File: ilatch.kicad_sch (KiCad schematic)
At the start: 11 parts, among them Q1 PNP, U25 74HC273, U26 74HC14, U27 74HC541, U28 74HC4075

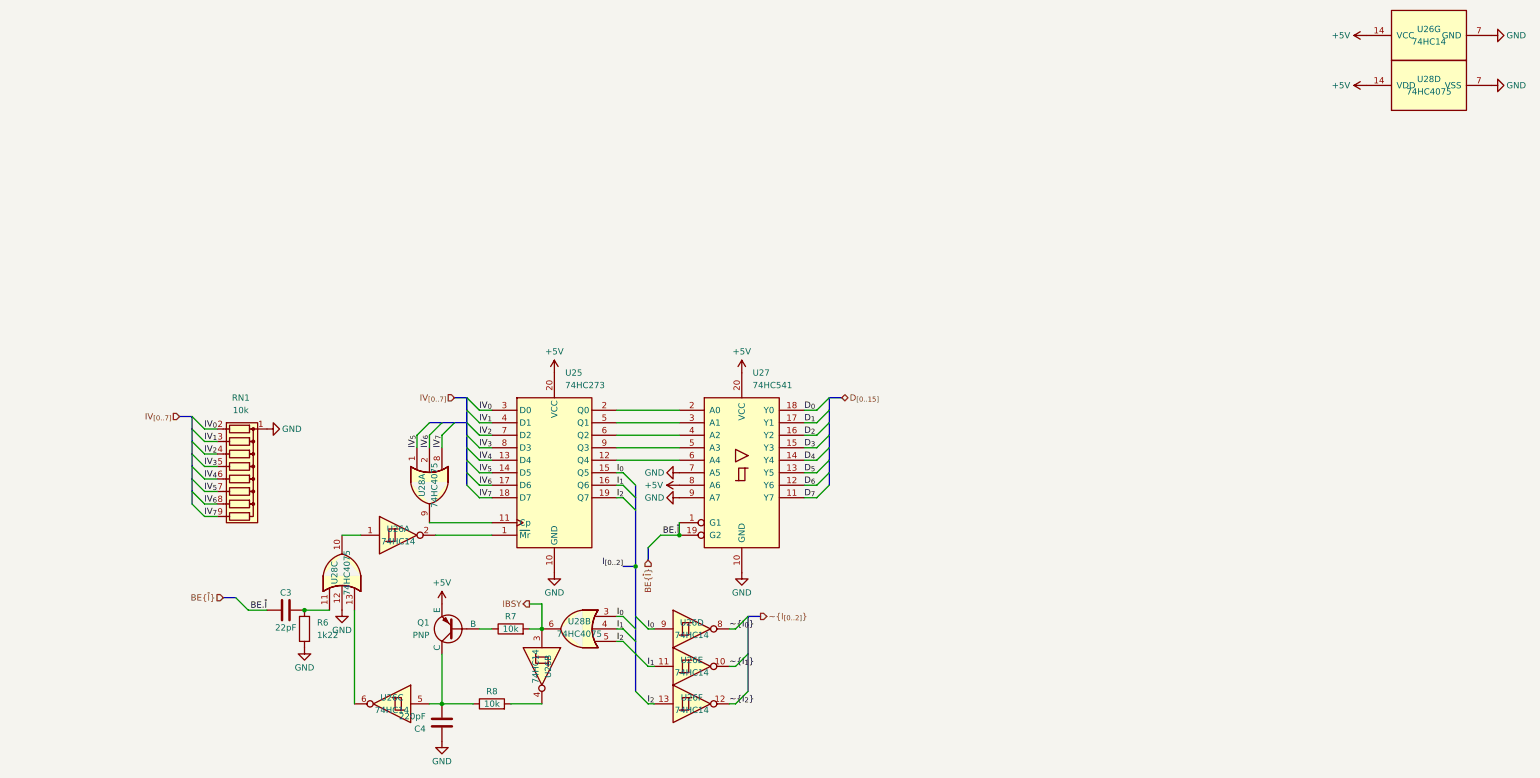
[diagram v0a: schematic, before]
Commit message: finished scheme, footprints not completely assigned yet
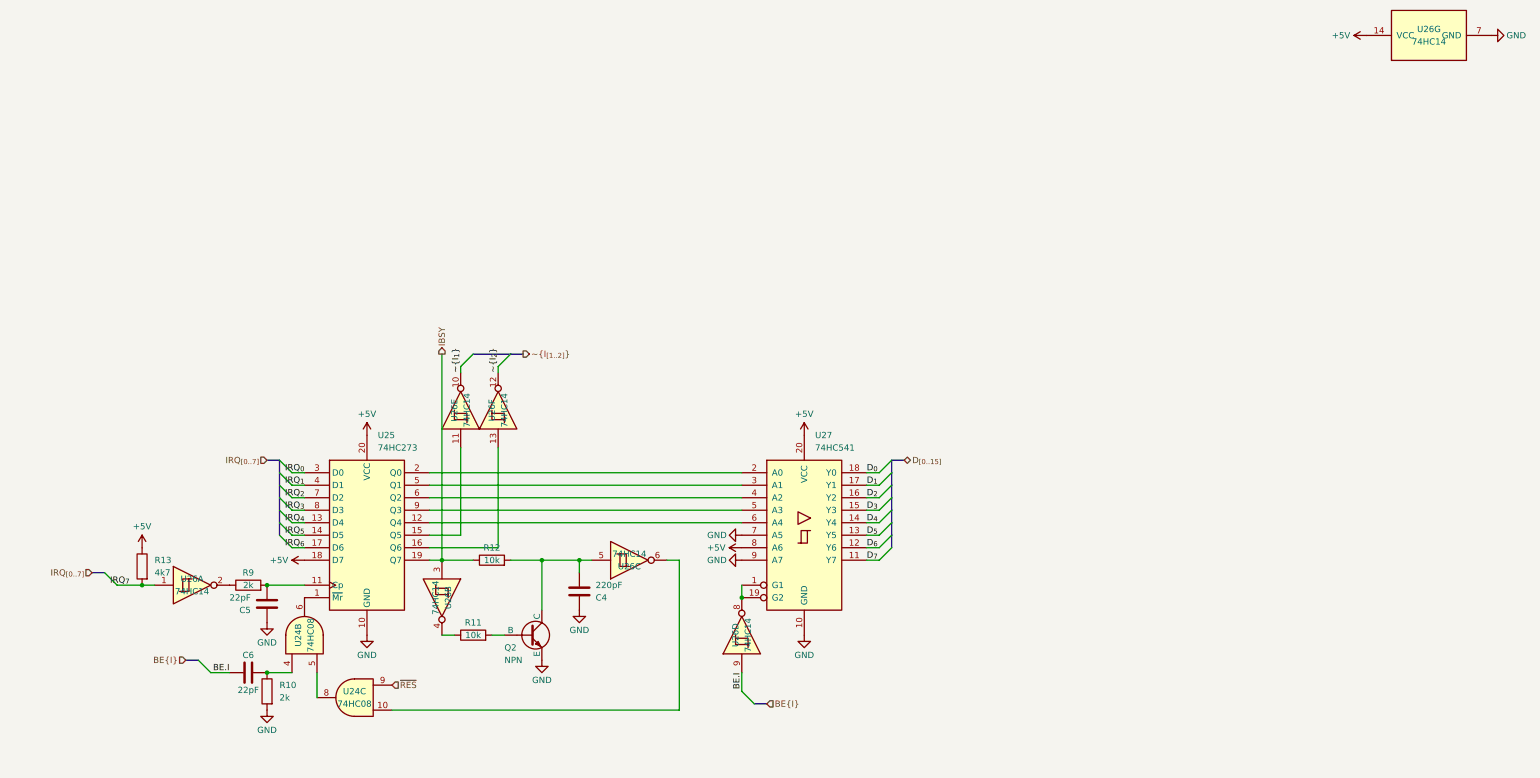
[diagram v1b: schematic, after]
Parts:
- removed C3: 22pF, Capacitor_THT:C_Disc_P2.54mm, symbol Device:C
- removed Q1: PNP, symbol Simulation_SPICE:PNP
- removed R6: 1k22, Resistor_THT:R_Axial_DIN0207_L6.3mm_D2.5mm_P2.54mm_Vertical, symbol Device:R
- removed R7, R8: 10k, Resistor_THT:R_Axial_DIN0207_L6.3mm_D2.5mm_P2.54mm_Vertical, symbol Device:R
- removed RN1: 10k, Resistor_THT:R_Array_SIP9, symbol Device:R_Network08
- removed U28: 74HC4075, Package_DIP:DIP-14_W7.62mm_Socket, symbol 4xxx:4075
- added C5, C6: 22pF, Capacitor_THT:C_Disc_P2.54mm, symbol Device:C
- added Q2: NPN, symbol Simulation_SPICE:NPN
- added R10, R9: 2k, Resistor_THT:R_Axial_DIN0207_L6.3mm_D2.5mm_P2.54mm_Vertical, symbol Device:R
- added R11, R12: 10k, Resistor_THT:R_Axial_DIN0207_L6.3mm_D2.5mm_P2.54mm_Vertical, symbol Device:R
- added R13: 4k7, Resistor_THT:R_Axial_DIN0207_L6.3mm_D2.5mm_P2.54mm_Vertical, symbol Device:R
- added U24: 74HC08, Package_DIP:DIP-14_W7.62mm_Socket, symbol 74xx:74LS08
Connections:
- net IV_{7} is gone; now on net +5V: U25.18 (D7)
- net ~{I_{0}} is gone; now on an unnamed net: U26.8
- net +5V: now also R13.1
- net GND: now also C5.1, Q2.3 (E), R10.2
- net IBSY: now also U25.19 (Q7), R12.1
- net IRQ_{7}: now reaches U26.1
- net IRQ_{7}: now also R13.2
- net at U26.2: now also R9.1; no longer U25.1 (~{Mr})
- net at U26.6: now also U24.10
- net at U26.4: now also R11.1
- net at C4.2, U26.5: now also Q2.1 (C), R12.2
- net at U25.11 (Cp): now also C5.2, R9.2
- net BE.~{I}: no longer names the net of U27.1 (G1), U27.19 (G2)
- net IV_{0} renamed IRQ_{0}
- net IV_{1} renamed IRQ_{1}
- net IV_{2} renamed IRQ_{2}
- net IV_{3} renamed IRQ_{3}
- net IV_{4} renamed IRQ_{4}
- net IV_{5} renamed IRQ_{5}
- net IV_{6} renamed IRQ_{6}
- net I_{0}: no longer names the net of U25.15 (Q5)
- net I_{0}: now also U26.11; no longer U26.9
- net I_{1}: no longer names the net of U25.16 (Q6)
- net I_{1}: now also U26.13; no longer U26.11
- removed net I_{2}: U25.19 (Q7), U26.13
- new net: C6.2, R10.1, U24.4
- new net: U24.5, U24.8
- new net: Q2.2 (B), R11.2
- new net: U24.6, U25.1 (~{Mr})
- new net BE.I: C6.1, U26.9
- new net ~{RES}: U24.9
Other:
- moved on the sheet: C4, U25, U26A, U26B, U26C, U26D, U26E, U26F, U27

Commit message: done the pcb layout + added the 1M ram bank project
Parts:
- C4, C5, C6: footprint Capacitor_THT:C_Disc_P2.54mm -> Capacitor_THT:C_Disc_D3.0mm_W1.6mm_P2.54mm
- Q2: footprint (none) -> Package_TO_SOT_THT:TO-92
- U24, U26: footprint Package_DIP:DIP-14_W7.62mm_Socket -> Package_DIP:DIP-14_W7.62mm
- U25: footprint (none) -> Package_DIP:DIP-20_W7.62mm
- U27: footprint Package_DIP:DIP-20_W7.62mm_Socket -> Package_DIP:DIP-20_W7.62mm
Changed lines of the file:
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@@
 			)
 		)
-		(property "Footprint" "Package_DIP:DIP-14_W7.62mm_Socket"
+		(property "Footprint" "Package_DIP:DIP-14_W7.62mm"
 			(at 78.74 111.76 0)
 			(effects
@@
 			)
 		)
-		(property "Footprint" "Capacitor_THT:C_Disc_P2.54mm"
+		(property "Footprint" "Capacitor_THT:C_Disc_D3.0mm_W1.6mm_P2.54mm"
 			(at 93.98 128.5748 0)
 			(effects
@@
 			)
 		)
-		(property "Footprint" "Package_DIP:DIP-14_W7.62mm_Socket"
+		(property "Footprint" "Package_DIP:DIP-14_W7.62mm"
 			(at 129.54 114.3 0)
 			(effects
@@
 			)
 		)
-		(property "Footprint" "Package_DIP:DIP-14_W7.62mm_Socket"
+		(property "Footprint" "Package_DIP:DIP-14_W7.62mm"
 			(at 111.76 134.62 0)
 			(effects
@@
 			)
 		)
-		(property "Footprint" "Package_DIP:DIP-14_W7.62mm_Socket"
+		(property "Footprint" "Package_DIP:DIP-14_W7.62mm"
 			(at 133.35 76.2 0)
 			(effects
@@
 			)
 		)
-		(property "Footprint" "Capacitor_THT:C_Disc_P2.54mm"
+		(property "Footprint" "Capacitor_THT:C_Disc_D3.0mm_W1.6mm_P2.54mm"
 			(at 156.5148 109.22 0)
 			(effects
@@
 			)
 		)
-		(property "Footprint" ""
+		(property "Footprint" "Package_TO_SOT_THT:TO-92"
 			(at 210.82 121.92 0)
 			(effects
@@
 			)
 		)
-		(property "Footprint" "Package_DIP:DIP-14_W7.62mm_Socket"
+		(property "Footprint" "Package_DIP:DIP-14_W7.62mm"
 			(at 140.97 76.2 0)
 			(effects
@@
 			)
 		)
-		(property "Footprint" "Package_DIP:DIP-20_W7.62mm_Socket"
+		(property "Footprint" "Package_DIP:DIP-20_W7.62mm"
 			(at 203.2 101.6 0)
 			(effects
@@
 			)
 		)
-		(property "Footprint" "Capacitor_THT:C_Disc_P2.54mm"
+		(property "Footprint" "Capacitor_THT:C_Disc_D3.0mm_W1.6mm_P2.54mm"
 			(at 94.9452 111.76 0)
 			(effects
@@
 			)
 		)
-		(property "Footprint" "Package_DIP:DIP-14_W7.62mm_Socket"
+		(property "Footprint" "Package_DIP:DIP-14_W7.62mm"
 			(at 190.5 121.92 0)
 			(effects
@@
 			)
 		)
-		(property "Footprint" ""
+		(property "Footprint" "Package_DIP:DIP-20_W7.62mm"
 			(at 114.3 101.6 0)
 			(effects
@@
 			)
 		)
-		(property "Footprint" "Package_DIP:DIP-14_W7.62mm_Socket"
+		(property "Footprint" "Package_DIP:DIP-14_W7.62mm"
 			(at 101.6 121.92 0)
 			(effects
@@
 			)
 		)
-		(property "Footprint" "Package_DIP:DIP-14_W7.62mm_Socket"
+		(property "Footprint" "Package_DIP:DIP-14_W7.62mm"
 			(at 167.64 106.68 0)
 			(effects
@@
 			)
 		)
-		(property "Footprint" "Package_DIP:DIP-14_W7.62mm_Socket"
+		(property "Footprint" "Package_DIP:DIP-14_W7.62mm"
 			(at 330.2 0 0)
 			(effects

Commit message: first commit: scheme ok [decoder]: 	- new spv. address space [mmu]: 	- removed pidreg 	- switched back to 8Kb mmu rams [ram/peripherals]: 	- added ground pins to connectors [misc]: 	- added DMA support 	- added clock halfer
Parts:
- added unit 3 of U31
- added unit 4 of U31
- added unit 5 of U31
- renumbered U24 to U31
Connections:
- net +5V: now also U31.10, U31.12, U31.13, U31.14 (VCC), U31.9
- net GND: now also U31.7 (GND)
- net ~{RES}: now also U31.4; no longer U31.9
- net at C6.2, R10.1: now also U31.1; no longer U31.4
- net at U26.6: now also U31.5; no longer U31.10
- net at U25.1 (~{Mr}): now also U31.3; no longer U31.6
- new net: U31.2, U31.6
- no-connect marks 0 -> 2

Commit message: applied sf68 & ps2 fixes stash from master
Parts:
- renumbered C6 to C5, R10 to R14
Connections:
- net +5V: now also R14.1
- net GND: no longer R14.2
- net at C5.2, U31.1: now also R14.2; no longer R14.1
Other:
- moved on the sheet: C5, R14
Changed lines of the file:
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@@
 	)
 	(junction
-		(at 322.58 40.64)
+		(at 129.54 106.68)
 		(diameter 0)
 		(color 0 0 0 0)
 	)
 	(junction
-		(at 93.98 129.54)
-		(diameter 0)
-		(color 0 0 0 0)
-	)
-	(junction
-		(at 129.54 106.68)
+		(at 93.98 139.7)
 		(diameter 0)
 		(color 0 0 0 0)
@@
 	)
 	(bus_entry
-		(at 80.01 127)
+		(at 80.01 137.16)
 		(size 2.54 2.54)
 		(stroke
@@
 	(wire
 		(pts
-			(xy 93.98 129.54) (xy 99.06 129.54)
+			(xy 93.98 139.7) (xy 99.06 139.7)
 		)
 		(stroke
@@
 	(wire
 		(pts
+			(xy 99.06 129.54) (xy 99.06 139.7)
+		)
+		(stroke
+			(width 0)
+			(type default)
+		)
+	)
+	(wire
+		(pts
 			(xy 127 101.6) (xy 133.35 101.6)
 		)
@@
 	(bus
 		(pts
-			(xy 77.47 127) (xy 80.01 127)
+			(xy 77.47 137.16) (xy 80.01 137.16)
 		)
 		(stroke
@@
 	(wire
 		(pts
-			(xy 82.55 129.54) (xy 86.36 129.54)
+			(xy 82.55 139.7) (xy 86.36 139.7)
 		)
 		(stroke
@@
 	)
 	(label "BE.I"
-		(at 86.36 129.54 180)
+		(at 86.36 139.7 180)
 		(effects
 			(font
@@
 	(hierarchical_label "BE{I}"
 		(shape input)
-		(at 77.47 127 180)
+		(at 77.47 137.16 180)
 		(effects
 			(font
@@
 	(symbol
 		(lib_id "Device:R")
-		(at 93.98 133.35 0)
+		(at 93.98 135.89 0)
 		(mirror y)
 		(unit 1)
@@
 		(on_board yes)
 		(dnp no)
-		(property "Reference" "R10"
-			(at 96.52 132.0799 0)
+		(property "Reference" "R14"
+			(at 96.52 134.6199 0)
 			(effects
 				(font
@@
 		)
 		(property "Value" "2k"
-			(at 96.52 134.6199 0)
+			(at 96.52 137.1599 0)
 			(effects
 				(font
@@
 		)
 		(property "Footprint" "Resistor_THT:R_Axial_DIN0207_L6.3mm_D2.5mm_P2.54mm_Vertical"
-			(at 95.758 133.35 90)
+			(at 95.758 135.89 90)
 			(effects
 				(font
@@
 			)
 		)
-		(property "Datasheet" "~"
-			(at 93.98 133.35 0)
+		(property "Datasheet" ""
+			(at 93.98 135.89 0)
 			(effects
 				(font
@@
 			)
 		)
-		(property "Description" "Resistor"
-			(at 93.98 133.35 0)
+		(property "Description" ""
+			(at 93.98 135.89 0)
 			(effects
 				(font
@@
 	)
 	(symbol
-		(lib_id "power:GND")
-		(at 93.98 137.16 0)
-		(mirror y)
-		(unit 1)
-		(exclude_from_sim no)
-		(in_bom yes)
-		(on_board yes)
-		(dnp no)
-		(property "Reference" "#PWR097"
-			(at 93.98 143.51 0)
-			(effects
-				(font
-					(size 1.27 1.27)
-				)
-				(hide yes)
-			)
-		)
-		(property "Value" "GND"
-			(at 93.98 141.224 0)
-			(effects
-				(font
-					(size 1.27 1.27)
-				)
-			)
-		)
-		(property "Footprint" ""
-			(at 93.98 137.16 0)
-			(effects
-				(font
-					(size 1.27 1.27)
-				)
-				(hide yes)
-			)
-		)
-		(property "Datasheet" ""
-			(at 93.98 137.16 0)
-			(effects
-				(font
-					(size 1.27 1.27)
-				)
-				(hide yes)
-			)
-		)
-		(property "Description" "Power symbol creates a global label with name \"GND\" , ground"
-			(at 93.98 137.16 0)
-			(effects
-				(font
-					(size 1.27 1.27)
-				)
-				(hide yes)
-			)
-		)
-		(pin "1"
-		)
-		(instances
-			(project "SCRM6816"
-				(path "/56448118-82b3-4e1c-bda3-84d63e01a14a/024e6e5e-a156-416a-80e5-bb61019b3b6b"
-					(reference "#PWR097")
-					(unit 1)
-				)
-			)
-		)
-	)
-	(symbol
 		(lib_id "power:+9V")
 		(at 101.6 106.68 90)
@@
 	(symbol
 		(lib_id "Device:C")
-		(at 90.17 129.54 90)
+		(at 90.17 139.7 90)
 		(unit 1)
 		(exclude_from_sim no)
@@
 		(on_board yes)
 		(dnp no)
-		(property "Reference" "C6"
-			(at 90.17 125.984 90)
+		(property "Reference" "C5"
+			(at 90.17 136.144 90)
 			(effects
 				(font
@@
 		)
 		(property "Value" "22pF"
-			(at 90.17 133.096 90)
+			(at 90.17 143.256 90)
 			(effects
 				(font
@@
 		)
 		(property "Footprint" "Capacitor_THT:C_Disc_D3.0mm_W1.6mm_P2.54mm"
-			(at 93.98 128.5748 0)
+			(at 93.98 138.7348 0)
 			(effects
 				(font
@@
 			)
 		)
-		(property "Datasheet" "~"
-			(at 90.17 129.54 0)
+		(property "Datasheet" ""
+			(at 90.17 139.7 0)
 			(effects
 				(font
@@
 			)
 		)
-		(property "Description" "Unpolarized capacitor"
-			(at 90.17 129.54 0)
+		(property "Description" ""
+			(at 90.17 139.7 0)
 			(effects
 				(font
@@
 					(unit 1)
 				)
+			)
+		)
+	)
+	(symbol
+		(lib_id "power:+9V")
+		(at 93.98 132.08 0)
+		(unit 1)
+		(exclude_from_sim no)
+		(in_bom yes)
+		(on_board yes)
+		(dnp no)
+		(property "Reference" "#PWR0224"
+			(at 93.98 135.89 0)
+			(effects
+				(font
+					(size 1.27 1.27)
+				)
+				(hide yes)
+			)
+		)
+		(property "Value" "+5V"
+			(at 93.98 127.762 0)
+			(effects
+				(font
+					(size 1.27 1.27)
+				)
+			)
+		)
+		(property "Footprint" ""
+			(at 93.98 132.08 0)
+			(effects
+				(font
+					(size 1.27 1.27)
+				)
+				(hide yes)
+			)
+		)
+		(property "Datasheet" ""
+			(at 93.98 132.08 0)
+			(effects
+				(font
+					(size 1.27 1.27)
+				)
+				(hide yes)
+			)
+		)
+		(property "Description" "Power symbol creates a global label with name \"+9V\""
+			(at 93.98 132.08 0)
+			(effects
+				(font
+					(size 1.27 1.27)
+				)
+				(hide yes)
+			)
+		)
+		(pin "1"
+		)
+		(instances
+			(project "SF68"
+				(path "/56448118-82b3-4e1c-bda3-84d63e01a14a/024e6e5e-a156-416a-80e5-bb61019b3b6b"
+					(reference "#PWR0224")
+					(unit 1)
+				)

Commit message: 1.0.0 commit
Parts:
- removed Q2: NPN, Package_TO_SOT_THT:TO-92, symbol Simulation_SPICE:NPN
- removed unit 3 of U31
- added Q1: Q_NPN_CBE, Package_TO_SOT_THT:TO-92, symbol Transistor_BJT:Q_NPN_CBE
- renumbered C5 to C2, C4 to C8, R9 to R12, R12 to R18, R11 to R19, U25 to U24, U31 to U25, U27 to U29, U26 to U30
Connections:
- net GND: now also Q1.3 (E)
- net at C8.2, R18.2, U30.5: now also Q1.1 (C)
- net at R19.2: now also Q1.2 (B)
- no-connect marks 2 -> 1
